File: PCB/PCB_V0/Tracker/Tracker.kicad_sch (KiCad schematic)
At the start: 16 parts, among them J1 Battery, J2 SPI_Programming, U1 L7805, U2 ATmega328P-P, U3 74HC123, Y1 16MHz

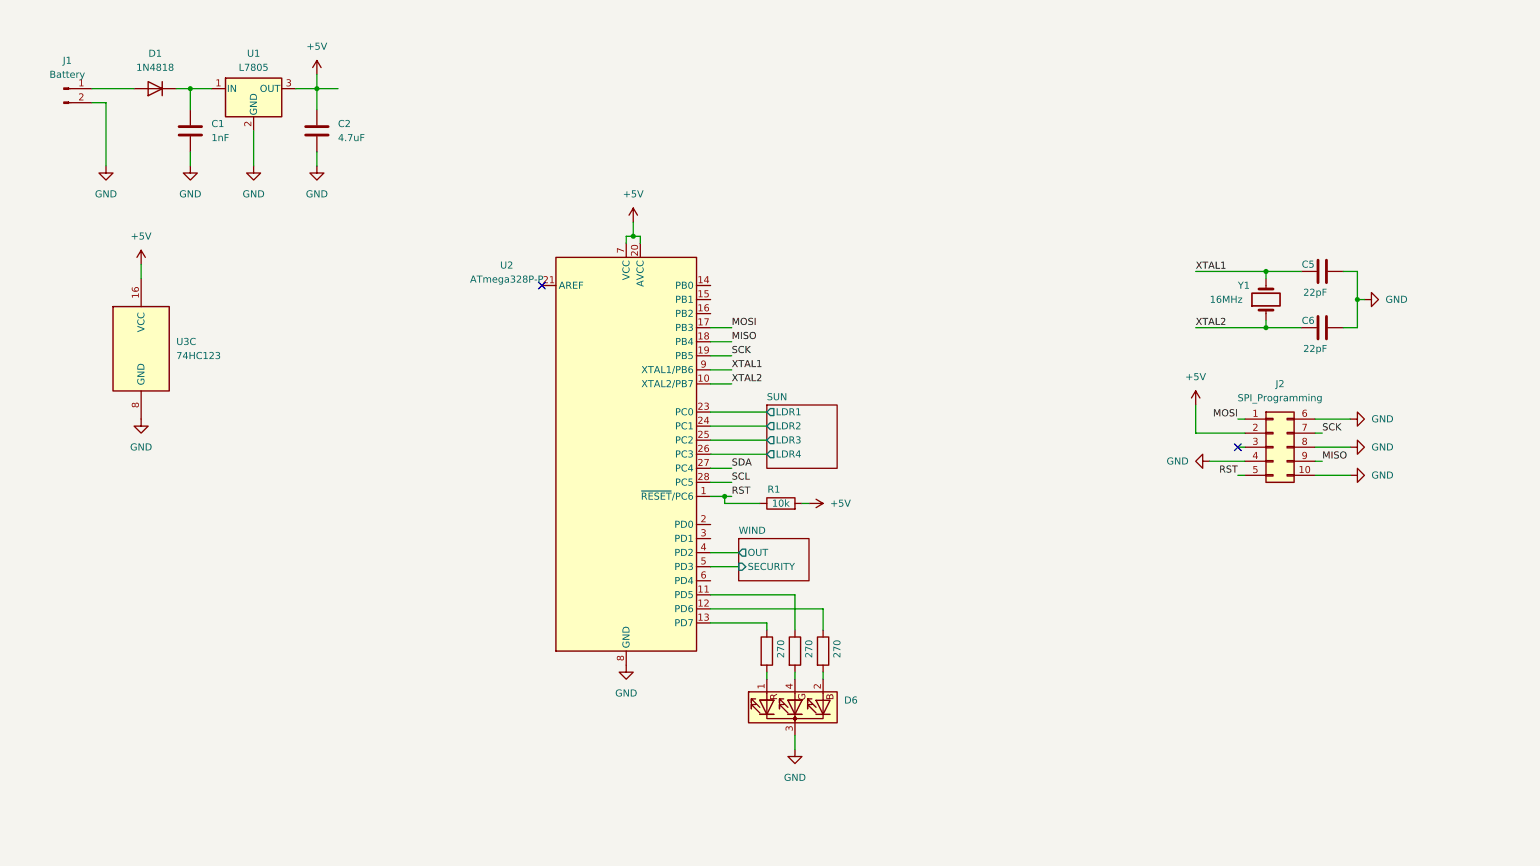
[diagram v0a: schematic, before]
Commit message: Add PCB with GNSS
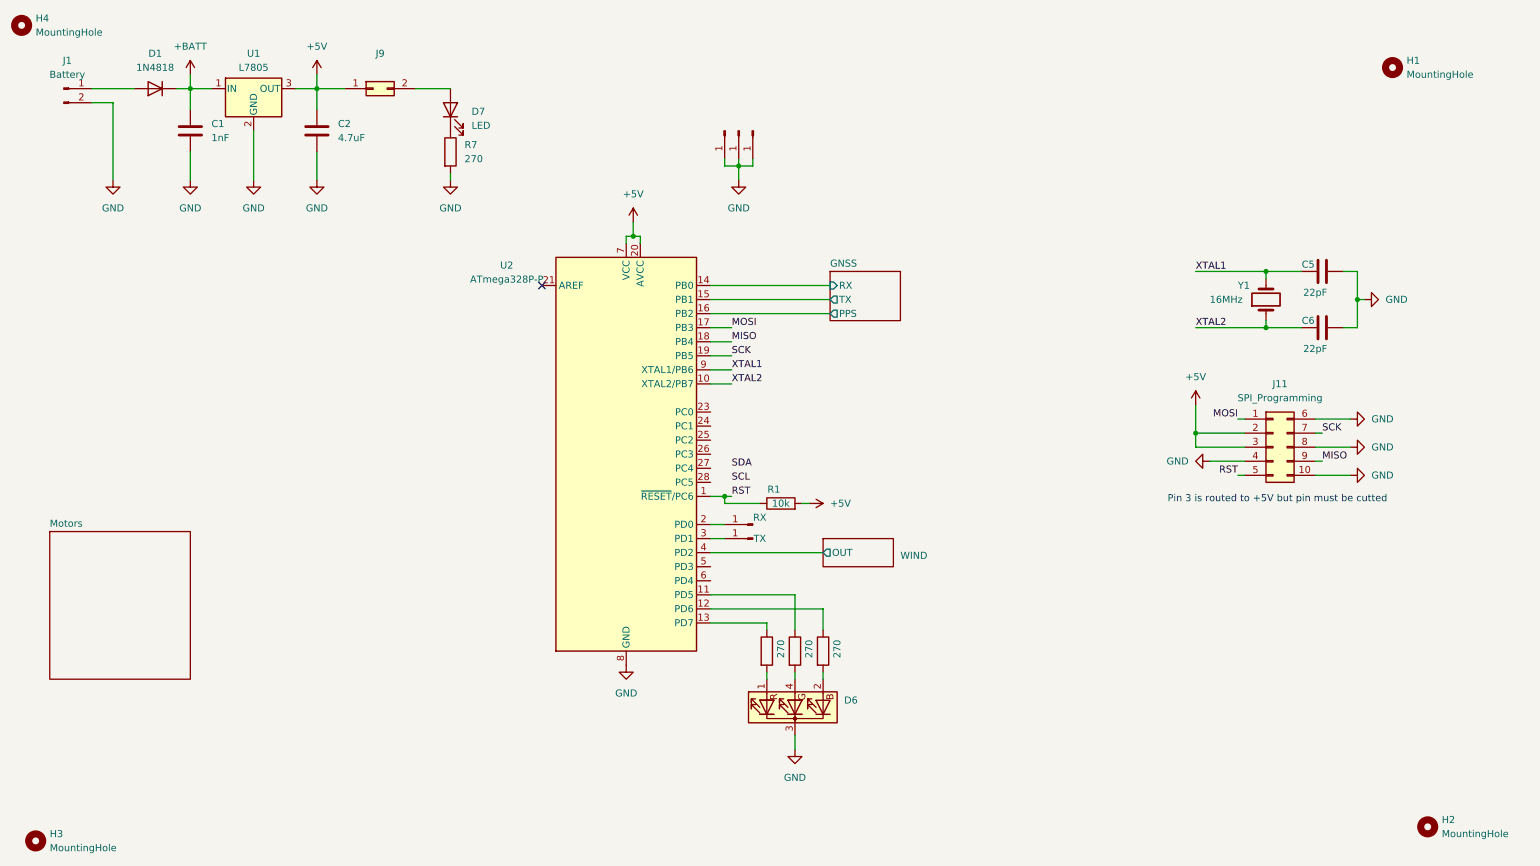
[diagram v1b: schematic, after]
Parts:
- removed J2: SPI_Programming, Connector_PinHeader_2.54mm:PinHeader_2x05_P2.54mm_Vertical, symbol Connector_Generic:Conn_02x05_Top_Bottom
- removed U3: 74HC123, Package_DIP:DIP-16_W7.62mm, symbol 74xx:74HC123
- added D7: LED, LED_THT:LED_D3.0mm, symbol Device:LED
- added H1, H2, H3, H4: MountingHole, MountingHole:MountingHole_3mm, symbol Mechanical:MountingHole
- added J11: SPI_Programming, Connector_PinHeader_2.54mm:PinHeader_2x05_P2.54mm_Vertical, symbol Connector_Generic:Conn_02x05_Top_Bottom
- added J4: RX, Connector_PinHeader_2.54mm:PinHeader_1x01_P2.54mm_Vertical, symbol Connector:Conn_01x01_Pin
- added J5: TX, Connector_PinHeader_2.54mm:PinHeader_1x01_P2.54mm_Vertical, symbol Connector:Conn_01x01_Pin
- added J6, J7, J8: GND, Connector_PinHeader_2.54mm:PinHeader_1x01_P2.54mm_Vertical, symbol Connector:Conn_01x01_Pin
- added J9: Haeder_LED, Connector_PinHeader_2.54mm:PinHeader_2x01_P2.54mm_Vertical, symbol Connector_Generic:Conn_02x01
- added R7: 270, Resistor_THT:R_Axial_DIN0204_L3.6mm_D1.6mm_P5.08mm_Horizontal, symbol Device:R
- J1: footprint Connector_Molex:Molex_KK-396_A-41791-0002_1x02_P3.96mm_Vertical -> TerminalBlock_Phoenix:TerminalBlock_Phoenix_MKDS-1,5-2-5.08_1x02_P5.08mm_Horizontal
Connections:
- net +5V: now also J11.2 (Pin_2), J11.3 (Pin_3), J9.1 (Pin_1)
- net GND: now also J11.10 (Pin_10), J11.4 (Pin_4), J11.6 (Pin_6), J11.8 (Pin_8), J6.1 (Pin_1), J7.1 (Pin_1), J8.1 (Pin_1), R7.2
- net MISO: now also J11.9 (Pin_9)
- net MOSI: now also J11.1 (Pin_1)
- net RST: now also J11.5 (Pin_5)
- net SCK: now also J11.7 (Pin_7)
- net SCL: no longer U2.28 (PC5)
- net SDA: no longer U2.27 (PC4)
- net GNSS/RX: now reaches U2.14 (PB0)
- net GNSS/TX: now reaches U2.15 (PB1)
- net GNSS/PPS: now reaches U2.16 (PB2)
- net at U2.2 (PD0): now also J4.1 (Pin_1)
- net at U2.3 (PD1): now also J5.1 (Pin_1)
- net +BATT: now reaches C1.1, D1.1 (K), U1.1 (IN)
- net SUN/LDR1: no longer names the net of U2.23 (PC0)
- net SUN/LDR2: no longer names the net of U2.24 (PC1)
- net SUN/LDR3: no longer names the net of U2.25 (PC2)
- net SUN/LDR4: no longer names the net of U2.26 (PC3)
- net WIND/SECURITY: no longer names the net of U2.5 (PD3)
- new net: D7.1 (K), R7.1
- new net: D7.2 (A), J9.2 (Pin_2)
- no-connect marks 2 -> 1
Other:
- removed sheet SUN
- added sheet GNSS (GNSS.kicad_sch)
- added sheet Motors (Motors.kicad_sch)
- sheet WIND ports: added none; removed SECURITY
- note added: "Pin 3 is routed to +5V but pin must be cutted"
